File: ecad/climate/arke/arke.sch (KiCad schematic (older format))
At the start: 4 parts, among them J1 MCV 1,5/ 2-G-3,5, J2 DB9_Female, J3 MCV 1,5/ 2-G-3,5, J5 MCV 1,5/ 2-G-3,5

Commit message: Updates Arke to KiCad 5
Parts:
- J1, J3, J5: footprint Connectors_Phoenix:PhoenixContact_MCV-G_02x3.50mm_Vertical -> Connector_Phoenix_MC:PhoenixContact_MCV_1,5_2-G-3.5_1x02_P3.50mm_Vertical; symbol Conn_01x02 -> Connector_Generic:Conn_01x02
- J2: symbol DB9_Female -> Connector:DB9_Female
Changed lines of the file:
@@
-EESchema Schematic File Version 2
+EESchema Schematic File Version 4
 LIBS:power
-LIBS:device
-LIBS:switches
-LIBS:relays
-LIBS:motors
-LIBS:transistors
-LIBS:conn
-LIBS:linear
-LIBS:regul
 LIBS:74xx
-LIBS:cmos4000
-LIBS:adc-dac
-LIBS:memory
-LIBS:xilinx
-LIBS:microcontrollers
-LIBS:dsp
-LIBS:microchip
-LIBS:analog_switches
-LIBS:motorola
-LIBS:texas
-LIBS:intel
-LIBS:audio
-LIBS:interface
-LIBS:digital-audio
-LIBS:philips
-LIBS:display
-LIBS:cypress
-LIBS:siliconi
-LIBS:opto
-LIBS:atmel
-LIBS:contrib
-LIBS:valves
 LIBS:fort
-LIBS:kerykeion-cache
-EELAYER 25 0
+LIBS:arke-cache
+EELAYER 26 0
 EELAYER END
 $Descr A4 11693 8268
@@
 $EndSheet
 $Sheet
-S 6250 3150 1650 350
+S 6400 3150 1650 350
 U 5BA1080F
 F0 "12V 5V Buck Converter" 60
 F1 "../../common/12V5VDCDC.sch" 60
-F2 "VIN" I R 7900 3300 60
-F3 "5V" O L 6250 3300 60
+F2 "VIN" I L 6400 3300 60
+F3 "5V" O R 8050 3300 60
 $EndSheet
 Wire Wire Line
@@
 	2050 3850 2350 3850
 Wire Wire Line
-	2350 3850 2350 4450
+	2350 3850 2350 4350
 Wire Wire Line
 	2350 4350 2050 4350
@@
 	2800 4250 2800 4200
 $Comp
-L +5V #PWR01
+L power:+5V #PWR01
 U 1 1 5BA2BA69
-P 5900 3250
-F 0 "#PWR01" H 5900 3100 50  0001 C CNN
-F 1 "+5V" H 5900 3390 50  0000 C CNN
-F 2 "" H 5900 3250 50  0001 C CNN
-F 3 "" H 5900 3250 50  0001 C CNN
-	1    5900 3250
-	1    0    0    -1
-$EndComp
-Wire Wire Line
-	5900 3250 5900 3300
-Wire Wire Line
-	5900 3300 6250 3300
-$Comp
-L +12V #PWR02
+P 8400 3250
+F 0 "#PWR01" H 8400 3100 50  0001 C CNN
+F 1 "+5V" H 8400 3390 50  0000 C CNN
+F 2 "" H 8400 3250 50  0001 C CNN
+F 3 "" H 8400 3250 50  0001 C CNN
+	1    8400 3250
+	-1   0    0    -1
+$EndComp
+Wire Wire Line
+	8400 3250 8400 3300
+Wire Wire Line
+	8400 3300 8050 3300
+$Comp
+L power:+12V #PWR02
 U 1 1 5BA2BB13
-P 8350 3200
-F 0 "#PWR02" H 8350 3050 50  0001 C CNN
-F 1 "+12V" H 8350 3340 50  0000 C CNN
-F 2 "" H 8350 3200 50  0001 C CNN
-F 3 "" H 8350 3200 50  0001 C CNN
-	1    8350 3200
-	1    0    0    -1
-$EndComp
-Wire Wire Line
-	8350 3200 8350 3300
-Wire Wire Line
-	8350 3300 7900 3300
-$Comp
-L Conn_01x02 J1
+P 5950 3200
+F 0 "#PWR02" H 5950 3050 50  0001 C CNN
+F 1 "+12V" H 5950 3340 50  0000 C CNN
+F 2 "" H 5950 3200 50  0001 C CNN
+F 3 "" H 5950 3200 50  0001 C CNN
+	1    5950 3200
+	-1   0    0    -1
+$EndComp
+Wire Wire Line
+	5950 3200 5950 3300
+Wire Wire Line
+	5950 3300 6400 3300
+$Comp
+L Connector_Generic:Conn_01x02 J1
 U 1 1 5BA2BBBF
 P 9900 3250
 F 0 "J1" H 9900 3350 50  0000 C CNN
 F 1 "MCV 1,5/ 2-G-3,5" H 9900 3050 50  0000 C CNN
-F 2 "Connectors_Phoenix:PhoenixContact_MCV-G_02x3.50mm_Vertical" H 9900 3250 50  0001 C CNN
+F 2 "Connector_Phoenix_MC:PhoenixContact_MCV_1,5_2-G-3.5_1x02_P3.50mm_Vertical" H 9900 3250 50  0001 C CNN
 F 3 "" H 9900 3250 50  0001 C CNN
 F 4 "MCV 1,5/ 2-G-3,5" H 9900 3250 60  0001 C CNN "Part Number"
@@
 $EndComp
 $Comp
-L +12V #PWR03
+L power:+12V #PWR03
 U 1 1 5BA2C21A
 P 9550 3100
@@
 $EndComp
 $Comp
-L GND #PWR04
+L power:GND #PWR04
 U 1 1 5BA2C362
 P 9550 3500
@@
 	9550 3250 9700 3250
 Wire Wire Line
-	7900 4150 9700 4150
+	7900 4150 9500 4150
 Wire Wire Line
 	9500 4150 9500 4550
@@
 	9500 4550 9700 4550
 Wire Wire Line
-	7900 4250 9700 4250
+	7900 4250 9600 4250
 Wire Wire Line
 	9600 4250 9600 4650
@@
 	3100 3650 2050 3650
 $Comp
-L Conn_01x02 J3
+L Connector_Generic:Conn_01x02 J3
 U 1 1 5BA38B3F
 P 9900 4150
 F 0 "J3" H 9900 4250 50  0000 C CNN
 F 1 "MCV 1,5/ 2-G-3,5" H 9900 3950 50  0000 C CNN
-F 2 "Connectors_Phoenix:PhoenixContact_MCV-G_02x3.50mm_Vertical" H 9900 4150 50  0001 C CNN
+F 2 "Connector_Phoenix_MC:PhoenixContact_MCV_1,5_2-G-3.5_1x02_P3.50mm_Vertical" H 9900 4150 50  0001 C CNN
 F 3 "" H 9900 4150 50  0001 C CNN
 F 4 "MCV 1,5/ 2-G-3,5" H 9900 4150 60  0001 C CNN "Part Number"
@@
 $EndComp
 $Comp
-L Conn_01x02 J5
+L Connector_Generic:Conn_01x02 J5
 U 1 1 5BA38BE4
 P 9900 4550
 F 0 "J5" H 9900 4650 50  0000 C CNN
 F 1 "MCV 1,5/ 2-G-3,5" H 9900 4350 50  0000 C CNN
-F 2 "Connectors_Phoenix:PhoenixContact_MCV-G_02x3.50mm_Vertical" H 9900 4550 50  0001 C CNN
+F 2 "Connector_Phoenix_MC:PhoenixContact_MCV_1,5_2-G-3.5_1x02_P3.50mm_Vertical" H 9900 4550 50  0001 C CNN
 F 3 "" H 9900 4550 50  0001 C CNN
 F 4 "MCV 1,5/ 2-G-3,5" H 9900 4550 60  0001 C CNN "Part Number"
@@
 $EndComp
 $Comp
-L DB9_Female J2
+L Connector:DB9_Female J2
 U 1 1 5BA3A8D5
 P 1750 4050
@@
 	-1   0    0    -1
 $EndComp
+Wire Wire Line
+	2350 4350 2350 4450
+Wire Wire Line
+	9500 4150 9700 4150
+Wire Wire Line
+	9600 4250 9700 4250
 $EndSCHEMATC

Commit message: Corrects issues on Arke
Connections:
- net RS232 Isolator/GND_ISO: now also J2.5; no longer J2.1
- net RS232 Isolator/ISO_TX: now also J2.2; no longer J2.4
- net at J2.6: now also J2.1, J2.4
- now unconnected: J2.9
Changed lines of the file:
@@
 F2 "CAN_TX" O R 6300 4150 60
 F3 "CAN_RX" I R 6300 4250 60
-F4 "UART_TX" O L 4950 4150 60
-F5 "UART_RX" I L 4950 4250 60
+F4 "UART_TX" O L 4950 4250 60
+F5 "UART_RX" I L 4950 4150 60
 $EndSheet
 $Sheet
@@
 F 4 "LD09S13A4GX00LF" H 1750 4050 60  0001 C CNN "Part Number"
 	1    1750 4050
-	-1   0    0    -1
+	-1   0    0    1
 $EndComp
 Wire Wire Line

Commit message: Licenses Climate PCB under OHL v1.2
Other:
- note added: "© 2018 Université de Lausanne\n\nThis documentation describes Open Hardware and is licensed under the\nCERN OHL v. 1.2.\n\nYou may redistribute and modify this documentation under the terms of\nthe CERN OHL v.1.2. (http://ohwr.org/cernohl). This documentation is\ndistributed WITHOUT ANY EXPRESS OR IMPLIED WARRANTY,\nINCLUDING OF MERCHANTABILITY, SATISFACTORY QUALITY AND\nFITNESS FOR A PARTICULAR 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"
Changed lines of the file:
@@
 encoding utf-8
 Sheet 1 5
-Title ""
-Date ""
-Rev ""
-Comp ""
-Comment1 ""
-Comment2 ""
+Title "Arke - RS232 <-> CAN Isolated Interface"
+Date "06/11/2018"
+Rev "A"
+Comp "Université de Lausanne"
+Comment1 "Author: Alexandre Tuleu"
+Comment2 "Licensed under the CERN OHL v1.2"
 Comment3 ""
 Comment4 ""
@@
 Wire Wire Line
 	9600 4250 9700 4250
+Text Notes 550  7750 0    50   ~ 0
+© 2018 Université de Lausanne\n\nThis documentation describes Open Hardware and is licensed under the\nCERN OHL v. 1.2.\n\nYou may redistribute and modify this documentation under the terms of\nthe CERN OHL v.1.2. (http://ohwr.org/cernohl). This documentation is\ndistributed WITHOUT ANY EXPRESS OR IMPLIED WARRANTY,\nINCLUDING OF MERCHANTABILITY, SATISFACTORY QUALITY AND\nFITNESS FOR A PARTICULAR PURPOSE. Please see the CERN OHL v.1.2\nfor applicable conditions
 $EndSCHEMATC

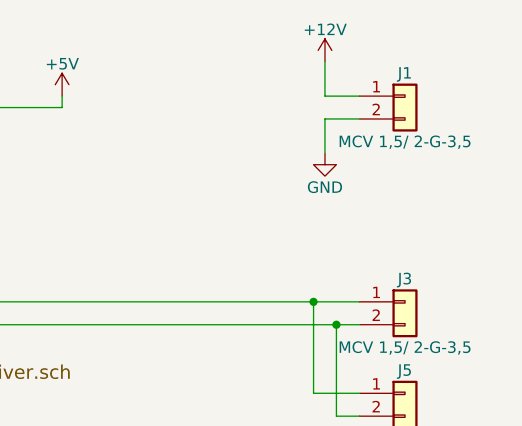
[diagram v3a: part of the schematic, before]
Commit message: Updates climate board to rev B~dev
 * Changes all Power Connectors to MiniFit-JR 5566-02A to avoid
   someone pluging the power supply on the CAN bus as it will destroy
   all MCP2561 on the bus
 * Fixes issues in Arke:
 ** Crossed Rx/Tx lines
 ** Flipped DB9 connector
 * Fixes and Improvment in Celaeno/Zeus:
 ** Added missing pull-up resistor on tachometer inputs
 ** Removed unecessary 32.268kHz oscillators (they are not working
    properly with manual soldering)
 ** Removed I2C multiplexer as we can add a second EMC2302 with a
   different i2c address to do the same thing. Repaced it by an i2c
   level shifter (tested and working).

Many of these changes still need to be tested before going to
production
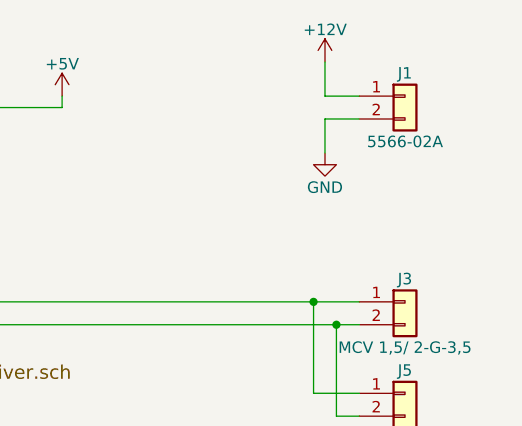
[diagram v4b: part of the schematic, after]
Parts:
- J1: value MCV 1,5/ 2-G-3,5 -> 5566-02A; footprint Connector_Phoenix_MC:PhoenixContact_MCV_1,5_2-G-3.5_1x02_P3.50mm_Vertical -> Connector_Molex:Molex_Mini-Fit_Jr_5566-02A_2x01_P4.20mm_Vertical; Part Number MCV 1,5/ 2-G-3,5 -> 39-28-1023
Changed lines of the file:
@@
 EESchema Schematic File Version 4
-LIBS:power
-LIBS:74xx
-LIBS:fort
 LIBS:arke-cache
 EELAYER 26 0
@@
 Title "Arke - RS232 <-> CAN Isolated Interface"
 Date "06/11/2018"
-Rev "A"
+Rev "B"
 Comp "Université de Lausanne"
 Comment1 "Author: Alexandre Tuleu"
@@
 P 9900 3250
 F 0 "J1" H 9900 3350 50  0000 C CNN
-F 1 "MCV 1,5/ 2-G-3,5" H 9900 3050 50  0000 C CNN
-F 2 "Connector_Phoenix_MC:PhoenixContact_MCV_1,5_2-G-3.5_1x02_P3.50mm_Vertical" H 9900 3250 50  0001 C CNN
+F 1 "5566-02A" H 9900 3050 50  0000 C CNN
+F 2 "Connector_Molex:Molex_Mini-Fit_Jr_5566-02A_2x01_P4.20mm_Vertical" H 9900 3250 50  0001 C CNN
 F 3 "" H 9900 3250 50  0001 C CNN
-F 4 "MCV 1,5/ 2-G-3,5" H 9900 3250 60  0001 C CNN "Part Number"
+F 4 "39-28-1023" H 9900 3250 60  0001 C CNN "Part Number"
 	1    9900 3250
 	1    0    0    -1

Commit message: Makes all electronics production ready
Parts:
- J1: footprint Connector_Molex:Molex_Mini-Fit_Jr_5566-02A_2x01_P4.20mm_Vertical -> FORT:Molex_Mini-Fit_Jr_5566-02A_2x01_P4.20mm_Vertical
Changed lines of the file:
@@
 F 0 "J1" H 9900 3350 50  0000 C CNN
 F 1 "5566-02A" H 9900 3050 50  0000 C CNN
-F 2 "Connector_Molex:Molex_Mini-Fit_Jr_5566-02A_2x01_P4.20mm_Vertical" H 9900 3250 50  0001 C CNN
+F 2 "FORT:Molex_Mini-Fit_Jr_5566-02A_2x01_P4.20mm_Vertical" H 9900 3250 50  0001 C CNN
 F 3 "" H 9900 3250 50  0001 C CNN
 F 4 "39-28-1023" H 9900 3250 60  0001 C CNN "Part Number"
